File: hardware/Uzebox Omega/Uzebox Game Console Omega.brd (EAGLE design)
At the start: 100 x 81 mm, 90 parts, among them CON1 USBSERIALSMD, IC1 MCP1700, IC2 7805T, K1 DC IN, K2 A/V, K5 ISP, K6 RCA-SWMULTICOMP, K7 RCA-SWMULTICOMP, U6 23LC1024

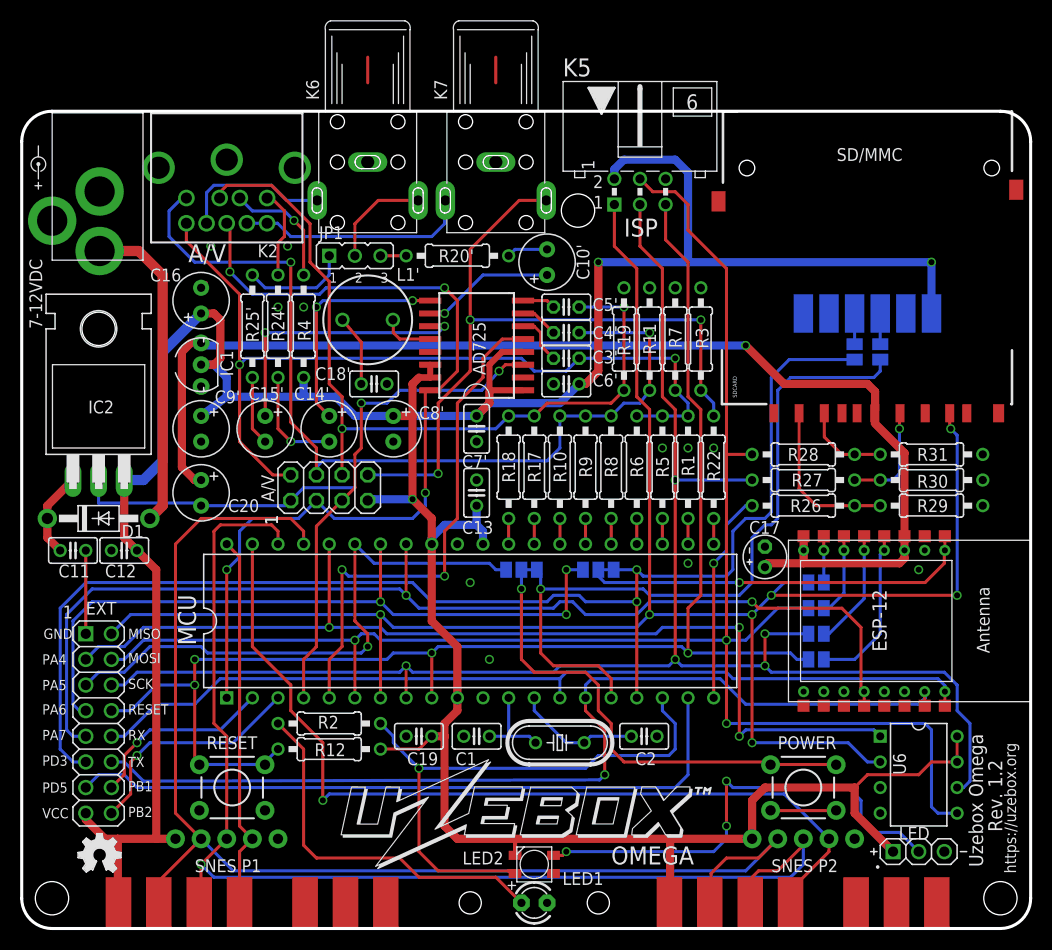
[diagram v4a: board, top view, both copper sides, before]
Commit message: Added optional uSD slot
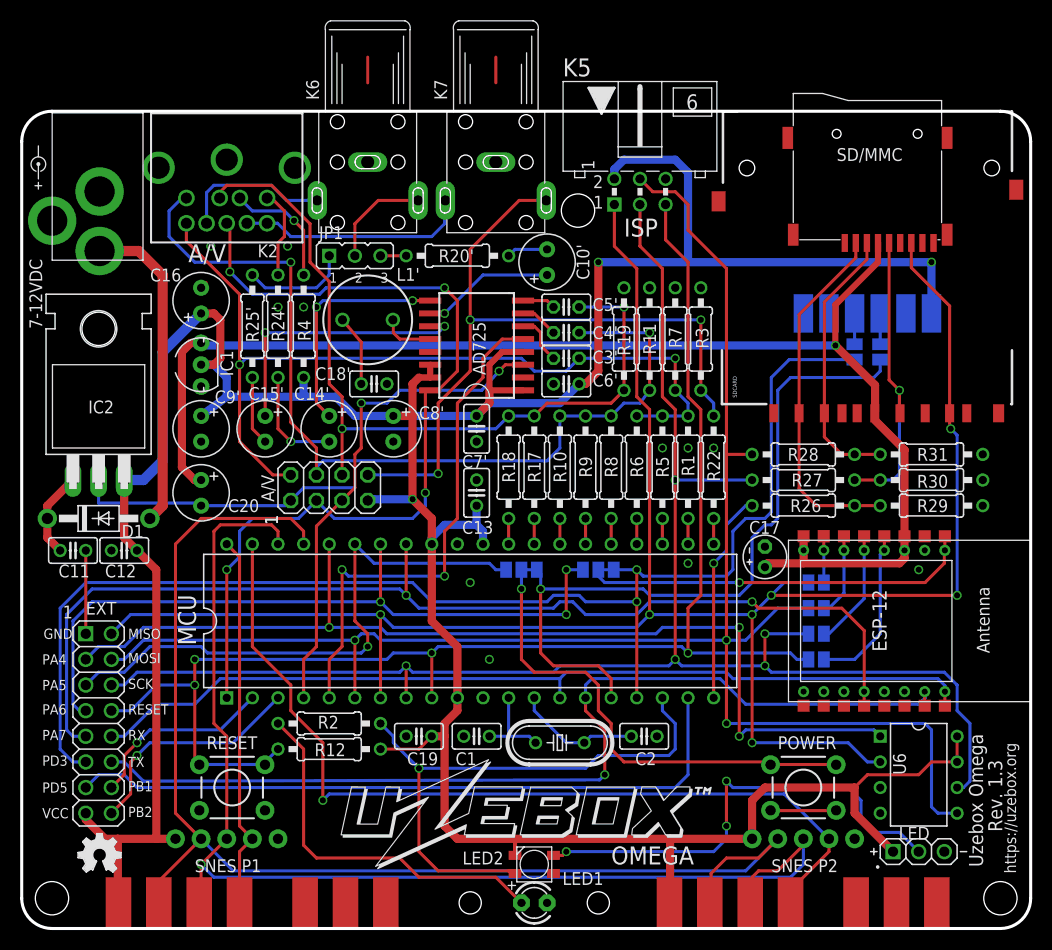
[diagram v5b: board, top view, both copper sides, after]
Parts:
- added J1: MICROSD-SWITCH, Thorsten_diverses:MICROSD-ATOM
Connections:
- net +3V3: now also J1.4
- net GND: now also J1.6
- net MISO: now also J1.7
- net MOSI_3V3: now also J1.3
- net SCK_3V3: now also J1.5
- net SD_CE_3V3: now also J1.2
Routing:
- net SCK_3V3: track 10.8 -> 30.5 mm
- net SD_CE_3V3: track 16.2 -> 35.4 mm
- net MOSI_3V3: track 8.61 -> 27.2 mm
- net MISO: track 185.5 -> 204.0 mm
- net +3V3: track 120.4 -> 132.6 mm
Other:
- board text added: "Rev. 1.3"
- board text removed: "Rev. 1.2"
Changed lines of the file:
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@@
 <text x="59.69" y="68.58" size="1.778" layer="21">ISP</text>
 <text x="58.42" y="6.35" size="1.778" layer="21">OMEGA</text>
-<text x="97.1865" y="9.5885" size="1.397" layer="21" font="vector" ratio="7" rot="R90">Rev. 1.2</text>
+<text x="97.1865" y="9.5885" size="1.397" layer="21" font="vector" ratio="7" rot="R90">Rev. 1.3</text>
 <text x="34.29" y="79.0575" size="1.778" layer="22" rot="SMR180" align="bottom-center">CVBS</text>
 <text x="46.99" y="79.0575" size="1.778" layer="22" rot="SMR180" align="bottom-center">Audio</text>
@@
 <element name="K6" library="Thorsten_connectors" package="CINCH_MULTICOMP" value="RCA-SWMULTICOMP" x="34.29" y="80.9625"/>
 <element name="K7" library="Thorsten_connectors" package="CINCH_MULTICOMP" value="RCA-SWMULTICOMP" x="46.99" y="80.9625"/>
+<element name="J1" library="Thorsten_diverses" package="MICROSD-ATOM" value="MICROSD-SWITCH" x="83.82" y="68.2625" rot="R180"/>
 </elements>
 <signals>
@@
 <contactref element="K2" pad="G2"/>
 <contactref element="K2" pad="G3"/>
+<contactref element="J1" pad="6"/>
 </signal>
 <signal name="G">
@@
 <wire x1="92.71" y1="33.02" x2="74.295" y2="33.02" width="0.3048" layer="1"/>
 <via x="74.295" y="33.02" extent="1-16" drill="0.6"/>
+<contactref element="J1" pad="7"/>
+<wire x1="88.17" y1="67.945" x2="88.17" y2="65.5" width="0.3048" layer="1"/>
+<wire x1="88.17" y1="65.5" x2="91.97" y2="61.7" width="0.3048" layer="1"/>
+<wire x1="91.97" y1="51.07" x2="91.97" y2="61.7" width="0.3048" layer="1"/>
 </signal>
 <signal name="SCK">
@@
 <contactref element="IC1" pad="3"/>
 <contactref element="C20" pad="+"/>
-<wire x1="17.399" y1="57.785" x2="71.755" y2="57.785" width="0.8128" layer="16"/>
-<wire x1="71.755" y1="57.785" x2="75.565" y2="53.975" width="0.8128" layer="1"/>
-<wire x1="75.565" y1="53.975" x2="83.82" y2="53.975" width="0.8128" layer="1"/>
+<wire x1="17.399" y1="57.785" x2="80.645" y2="57.785" width="0.8128" layer="16"/>
+<wire x1="80.645" y1="57.785" x2="84.582" y2="53.848" width="0.8128" layer="1"/>
 <wire x1="17.78" y1="58.039" x2="17.399" y2="57.785" width="0.3048" layer="16"/>
 <wire x1="15.875" y1="45.72" x2="15.875" y2="57.15" width="0.8128" layer="1"/>
@@
 <wire x1="17.78" y1="44.45" x2="17.145" y2="44.45" width="0.8128" layer="1"/>
 <wire x1="17.145" y1="44.45" x2="15.875" y2="45.72" width="0.8128" layer="1"/>
-<wire x1="84.582" y1="51.308" x2="84.582" y2="53.213" width="0.8128" layer="1"/>
-<wire x1="84.582" y1="53.213" x2="83.82" y2="53.975" width="0.8128" layer="1"/>
+<wire x1="84.582" y1="51.308" x2="84.582" y2="53.848" width="0.8128" layer="1"/>
 <contactref element="ESP-12" pad="8"/>
 <contactref element="ESP-12" pad="3"/>
@@
 <contactref element="ESP-12" pad="P$3"/>
 <contactref element="ESP-12" pad="P$8"/>
-<wire x1="87.495" y1="38.88" x2="87.5" y2="47.12" width="0.8128" layer="1"/>
-<wire x1="84.55" y1="51.07" x2="84.55" y2="50.07" width="0.3048" layer="1"/>
-<wire x1="84.55" y1="50.07" x2="87.5" y2="47.12" width="0.8128" layer="1"/>
+<wire x1="87.495" y1="38.88" x2="87.5" y2="47.4375" width="0.8128" layer="1"/>
+<wire x1="84.55" y1="51.07" x2="84.55" y2="50.3875" width="0.3048" layer="1"/>
+<wire x1="84.55" y1="50.3875" x2="87.5" y2="47.4375" width="0.8128" layer="1"/>
 <wire x1="87.495" y1="38.88" x2="87.495" y2="37.48" width="0.8128" layer="1"/>
 <wire x1="87.495" y1="37.48" x2="87.5" y2="36.7" width="0.8128" layer="1"/>
@@
 <wire x1="15.875" y1="57.15" x2="16.764" y2="58.039" width="0.8128" layer="1"/>
 <wire x1="16.764" y1="58.039" x2="17.78" y2="58.039" width="0.8128" layer="1"/>
-<via x="71.755" y="57.785" extent="1-16" drill="0.6"/>
+<via x="80.645" y="57.785" extent="1-16" drill="0.6"/>
+<contactref element="J1" pad="4"/>
+<wire x1="84.87" y1="67.945" x2="84.87" y2="66.04" width="0.6096" layer="1"/>
+<wire x1="80.645" y1="57.785" x2="80.645" y2="61.815" width="0.6096" layer="1"/>
+<wire x1="80.645" y1="61.815" x2="84.87" y2="66.04" width="0.6096" layer="1"/>
 </signal>
 <signal name="RESET">
@@
 <wire x1="81.28" y1="46.99" x2="82.55" y2="46.99" width="0.3048" layer="1"/>
 <wire x1="82.55" y1="46.99" x2="85.09" y2="46.99" width="0.3048" layer="1"/>
+<contactref element="J1" pad="3"/>
+<wire x1="83.77" y1="67.945" x2="83.77" y2="66.3075" width="0.3048" layer="1"/>
+<wire x1="83.77" y1="66.3075" x2="79.55" y2="62.0875" width="0.3048" layer="1"/>
+<wire x1="79.55" y1="51.07" x2="79.55" y2="62.0875" width="0.3048" layer="1"/>
 </signal>
 <signal name="SCK_3V3">
@@
 <wire x1="85.09" y1="44.45" x2="86.36" y2="44.45" width="0.3048" layer="16"/>
 <wire x1="86.36" y1="44.45" x2="86.995" y2="45.085" width="0.3048" layer="16"/>
-<wire x1="86.995" y1="45.085" x2="86.995" y2="49.53" width="0.3048" layer="16"/>
-<via x="86.995" y="49.53" extent="1-16" drill="0.6"/>
-<wire x1="86.995" y1="49.53" x2="86.995" y2="51.015" width="0.3048" layer="1"/>
+<wire x1="86.995" y1="45.085" x2="86.995" y2="53.34" width="0.3048" layer="16"/>
+<via x="86.995" y="53.34" extent="1-16" drill="0.6"/>
+<wire x1="86.995" y1="53.34" x2="86.995" y2="51.015" width="0.3048" layer="1"/>
 <wire x1="86.995" y1="51.015" x2="87.05" y2="51.07" width="0.3048" layer="1"/>
 <wire x1="82.55" y1="44.45" x2="85.09" y2="44.45" width="0.3048" layer="1"/>
+<contactref element="J1" pad="5"/>
+<wire x1="85.97" y1="67.945" x2="85.97" y2="54.365" width="0.3048" layer="1"/>
+<wire x1="85.97" y1="54.365" x2="86.995" y2="53.34" width="0.3048" layer="1"/>
 </signal>
 <signal name="SD_CE_3V3">
@@
 <wire x1="78.74" y1="41.91" x2="82.55" y2="41.91" width="0.3048" layer="1"/>
 <wire x1="82.55" y1="41.91" x2="85.09" y2="41.91" width="0.3048" layer="1"/>
+<contactref element="J1" pad="2"/>
+<wire x1="82.67" y1="67.945" x2="82.67" y2="66.4775" width="0.3048" layer="1"/>
+<wire x1="82.67" y1="66.4775" x2="77.05" y2="60.8575" width="0.3048" layer="1"/>
+<wire x1="77.05" y1="51.07" x2="77.05" y2="60.8575" width="0.3048" layer="1"/>
 </signal>
 <signal name="SD_CE">
@@
 <wire x1="72.39" y1="32.385" x2="73.025" y2="31.75" width="0.3048" layer="1"/>
 <wire x1="73.025" y1="31.75" x2="81.28" y2="31.75" width="0.3048" layer="1"/>
-<wire x1="81.28" y1="31.75" x2="83.185" y2="29.845" width="0.3048" layer="1"/>
+<wire x1="81.28" y1="31.75" x2="83.5025" y2="29.5275" width="0.3048" layer="1"/>
 <wire x1="38.1" y1="38.1" x2="38.1" y2="33.02" width="0.3048" layer="1"/>
 <via x="38.1" y="33.02" extent="1-16" drill="0.6"/>
@@
 <contactref element="ESP-12" pad="P$12"/>
 <wire x1="83.495" y1="22.08" x2="83.495" y2="23.48" width="0.3048" layer="1"/>
-<wire x1="83.185" y1="29.845" x2="83.185" y2="23.815" width="0.3048" layer="1"/>
-<wire x1="83.185" y1="23.815" x2="83.495" y2="23.48" width="0.3048" layer="1"/>
+<wire x1="83.5025" y1="29.5275" x2="83.5025" y2="23.4975" width="0.3048" layer="1"/>
+<wire x1="83.5025" y1="23.4975" x2="83.495" y2="23.48" width="0.3048" layer="1"/>
 <wire x1="4.445" y1="19.685" x2="5.08" y2="19.05" width="0.3048" layer="16"/>
 <wire x1="5.08" y1="19.05" x2="6.35" y2="19.05" width="0.3048" layer="16"/>

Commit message: Corrected footprint for RCA sockets
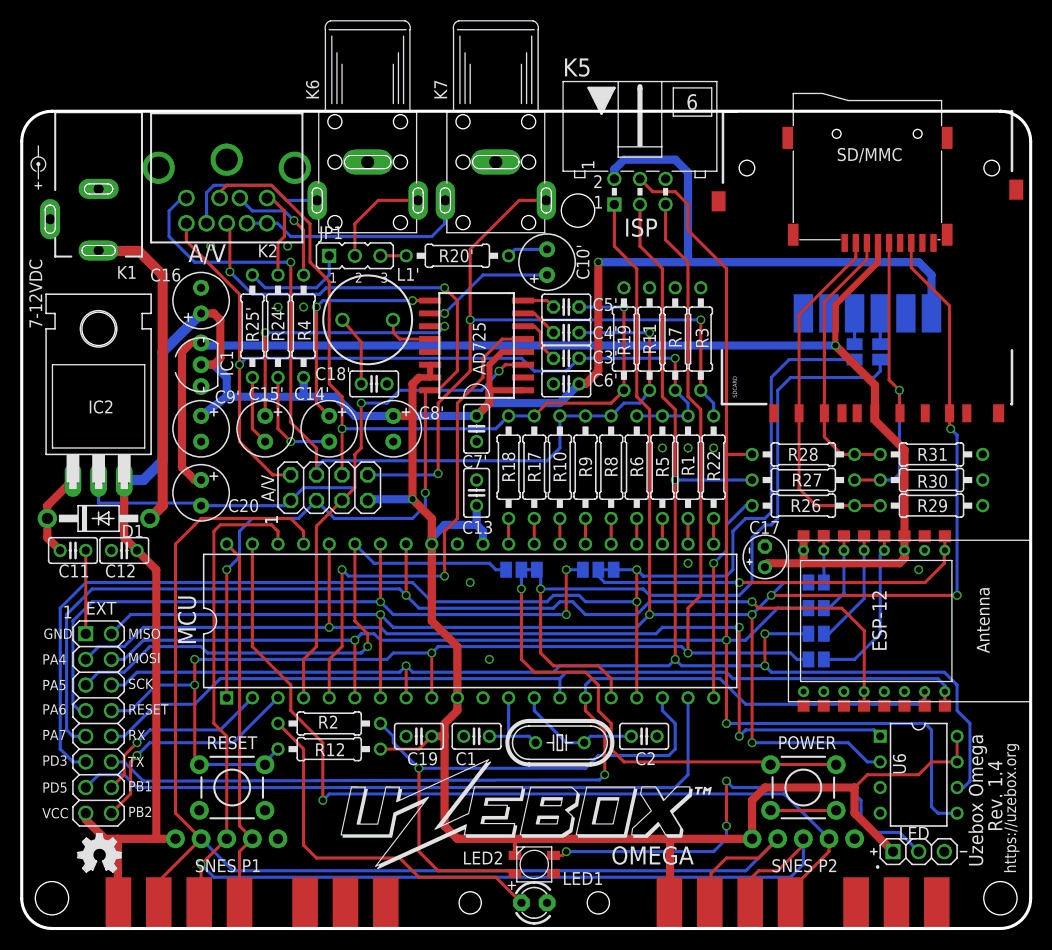
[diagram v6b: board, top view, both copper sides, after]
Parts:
- K1: value DC IN -> 9..12V DC; device adafruit:PJ-102A -> Thorsten_connectors:DCJACK
- moved K1 4.46 mm to (7.62, 80.9)
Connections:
- net GND: now also K1.3; no longer K1.RING
- net N$10: now also K1.1; no longer K1.TIP
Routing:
- net N$16: track 2.54 -> 0.00 mm
- net N$14: track 2.54 -> 0.00 mm
- net +5V: track 359.5 -> 358.8 mm, vias 3 -> 2
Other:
- board text added: "RGB"
- board text added: "Rev. 1.4"
- board text removed: "Rev. 1.3"
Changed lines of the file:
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@@
 <text x="59.69" y="68.58" size="1.778" layer="21">ISP</text>
 <text x="58.42" y="6.35" size="1.778" layer="21">OMEGA</text>
-<text x="97.1865" y="9.5885" size="1.397" layer="21" font="vector" ratio="7" rot="R90">Rev. 1.3</text>
+<text x="97.1865" y="9.5885" size="1.397" layer="21" font="vector" ratio="7" rot="R90">Rev. 1.4</text>
 <text x="34.29" y="79.0575" size="1.778" layer="22" rot="SMR180" align="bottom-center">CVBS</text>
 <text x="46.99" y="79.0575" size="1.778" layer="22" rot="SMR180" align="bottom-center">Audio</text>
-<text x="20.32" y="80.01" size="1.778" layer="22" rot="SMR180" align="bottom-center">9V DC</text>
+<text x="7.62" y="80.01" size="1.778" layer="22" rot="SMR180" align="bottom-center">9V DC</text>
 <text x="61.2775" y="79.375" size="1.778" layer="22" rot="SMR180" align="bottom-center">ISP</text>
+<text x="20.32" y="80.01" size="1.778" layer="22" rot="SMR180" align="bottom-center">RGB</text>
 </plain>
 <attributes>
@@
 <attribute name="VALUE" x="45.4406" y="67.31" size="1.27" layer="27" ratio="10" rot="R180"/>
 </element>
-<element name="K1" library="adafruit" package="PJ-102A" value="DC IN" x="7.62" y="76.438" smashed="yes">
-<attribute name="LABEL" value="DC IN (9-12V)" x="7.62" y="76.438" size="1.778" layer="27" display="off"/>
-</element>
 <element name="D1" library="adafruit" package="DO41-10" value="1N4001" x="7.62" y="40.64" smashed="yes">
 <attribute name="NAME" x="9.906" y="38.735" size="1.27" layer="21" font="vector" ratio="10"/>
@@
 <element name="K7" library="Thorsten_connectors" package="CINCH_MULTICOMP" value="RCA-SWMULTICOMP" x="46.99" y="80.9625"/>
 <element name="J1" library="Thorsten_diverses" package="MICROSD-ATOM" value="MICROSD-SWITCH" x="83.82" y="68.2625" rot="R180"/>
+<element name="K1" library="Thorsten_connectors" package="DCJACK" value="9..12V DC" x="7.62" y="80.9"/>
 </elements>
 <signals>
@@
 <contactref element="SNES_P2" pad="P$14"/>
 <contactref element="SNES_P1" pad="P$14"/>
-<contactref element="K1" pad="RING"/>
 <contactref element="C11" pad="2"/>
 <contactref element="C12" pad="2"/>
@@
 <contactref element="K2" pad="G3"/>
 <contactref element="J1" pad="6"/>
+<contactref element="K1" pad="3"/>
 </signal>
 <signal name="G">
@@
 </signal>
 <signal name="N$10">
-<contactref element="K1" pad="TIP"/>
 <contactref element="D1" pad="A"/>
 <wire x1="12.7" y1="40.64" x2="13.97" y2="41.91" width="1.016" layer="1"/>
 <wire x1="13.97" y1="41.91" x2="13.97" y2="64.77" width="1.016" layer="1"/>
-<wire x1="7.72" y1="67.148" x2="11.592" y2="67.148" width="1.016" layer="1"/>
 <wire x1="11.592" y1="67.148" x2="13.97" y2="64.77" width="1.016" layer="1"/>
+<contactref element="K1" pad="1"/>
+<wire x1="11.592" y1="67.148" x2="7.62" y2="67.148" width="1.016" layer="1"/>
+<wire x1="7.62" y1="67.148" x2="7.62" y2="67.2" width="1.016" layer="1"/>
 </signal>
 <signal name="N$9">
@@
 <wire x1="38.735" y1="53.975" x2="38.735" y2="50.8" width="0.8128" layer="1"/>
 <contactref element="CON1" pad="P-5V"/>
-<wire x1="90.17" y1="60.96" x2="90.17" y2="66.04" width="0.8128" layer="16"/>
-<via x="90.17" y="66.04" extent="1-16" drill="0.6"/>
-<wire x1="90.17" y1="66.04" x2="66.04" y2="66.04" width="0.8128" layer="16"/>
+<wire x1="90.17" y1="60.96" x2="90.17" y2="64.77" width="0.8128" layer="16"/>
+<wire x1="90.17" y1="64.77" x2="88.9" y2="66.04" width="0.8128" layer="16"/>
+<wire x1="88.9" y1="66.04" x2="66.04" y2="66.04" width="0.8128" layer="16"/>
 <via x="57.15" y="66.04" extent="1-16" drill="0.6"/>
 <contactref element="K5" pad="2"/>
@@
 <wire x1="29.29" y1="72.1625" x2="26.2625" y2="72.1625" width="0.3048" layer="16"/>
 </signal>
-<signal name="N$14">
-<wire x1="34.29" y1="83.82" x2="34.29" y2="86.36" width="0.3048" layer="1"/>
-</signal>
-<signal name="N$16">
-<wire x1="46.99" y1="83.82" x2="46.99" y2="86.36" width="0.3048" layer="1"/>
-</signal>
 <signal name="N$8">
